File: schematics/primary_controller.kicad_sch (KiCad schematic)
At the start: 0 parts

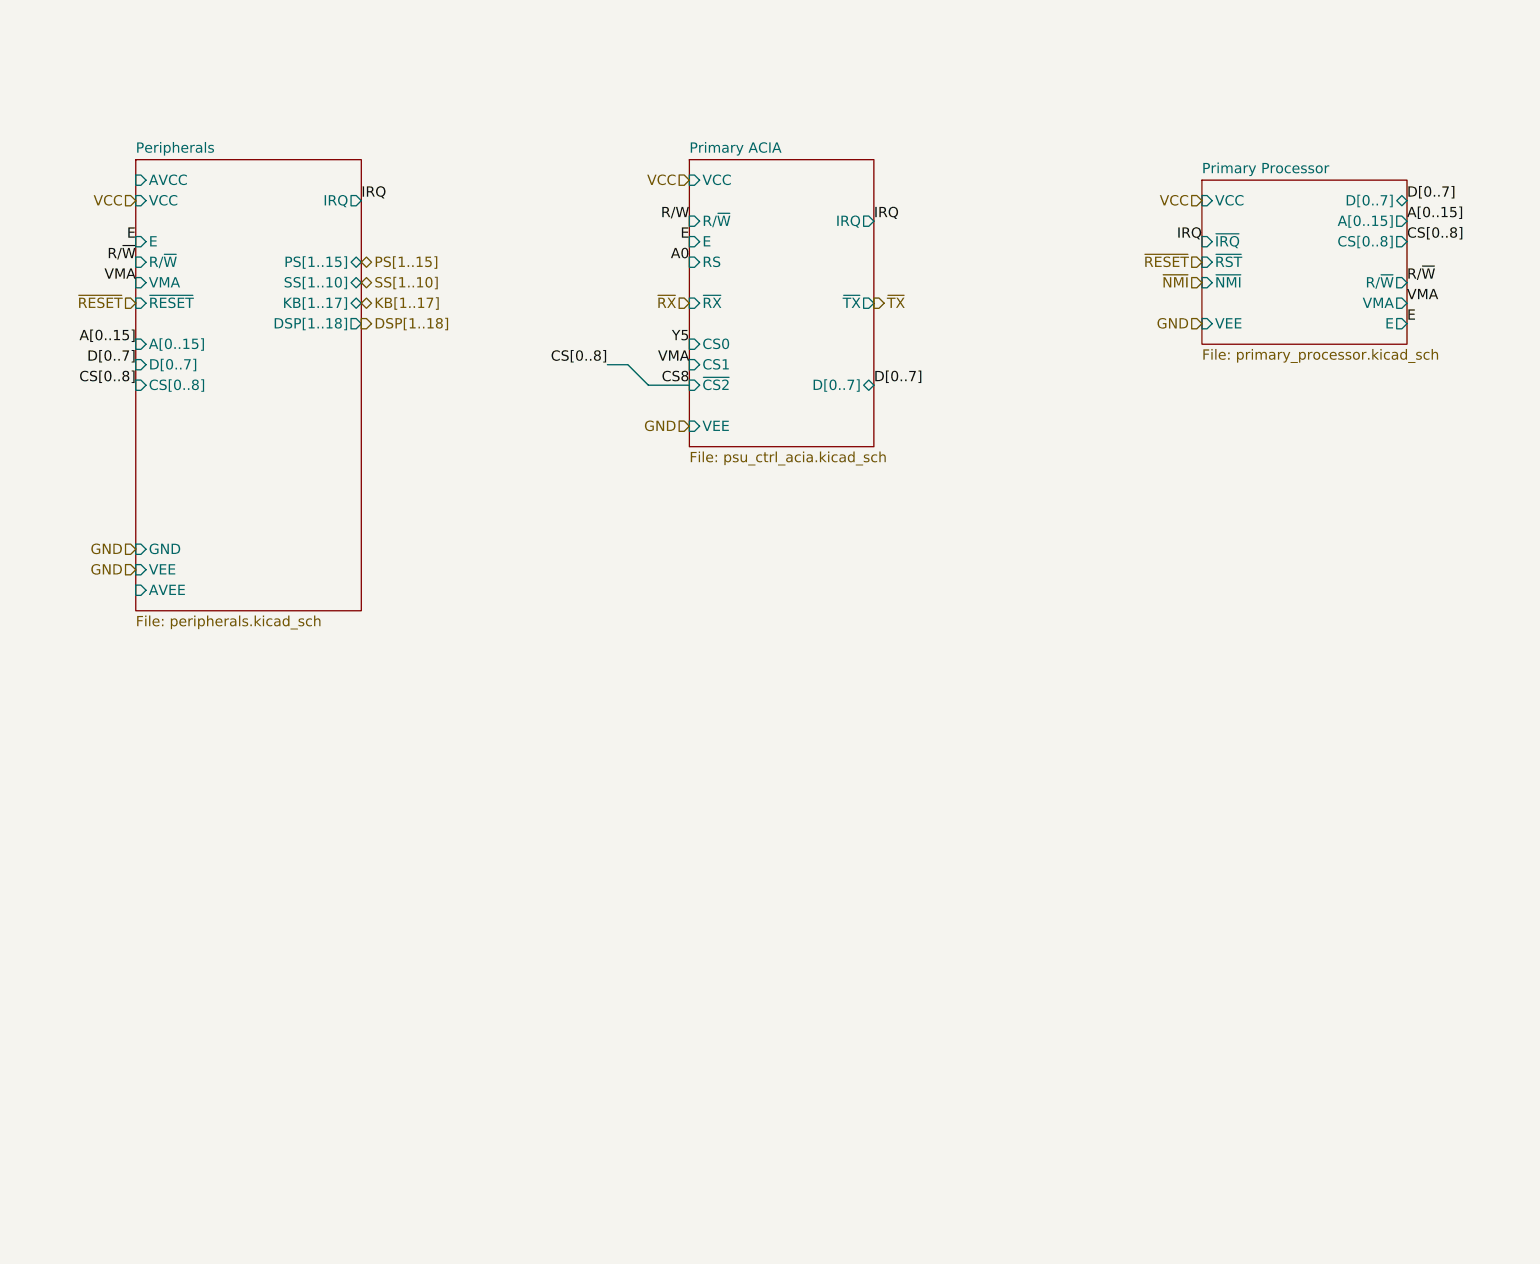
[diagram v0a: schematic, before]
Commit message: Moved more components into hierachical sheets, misc cleanup
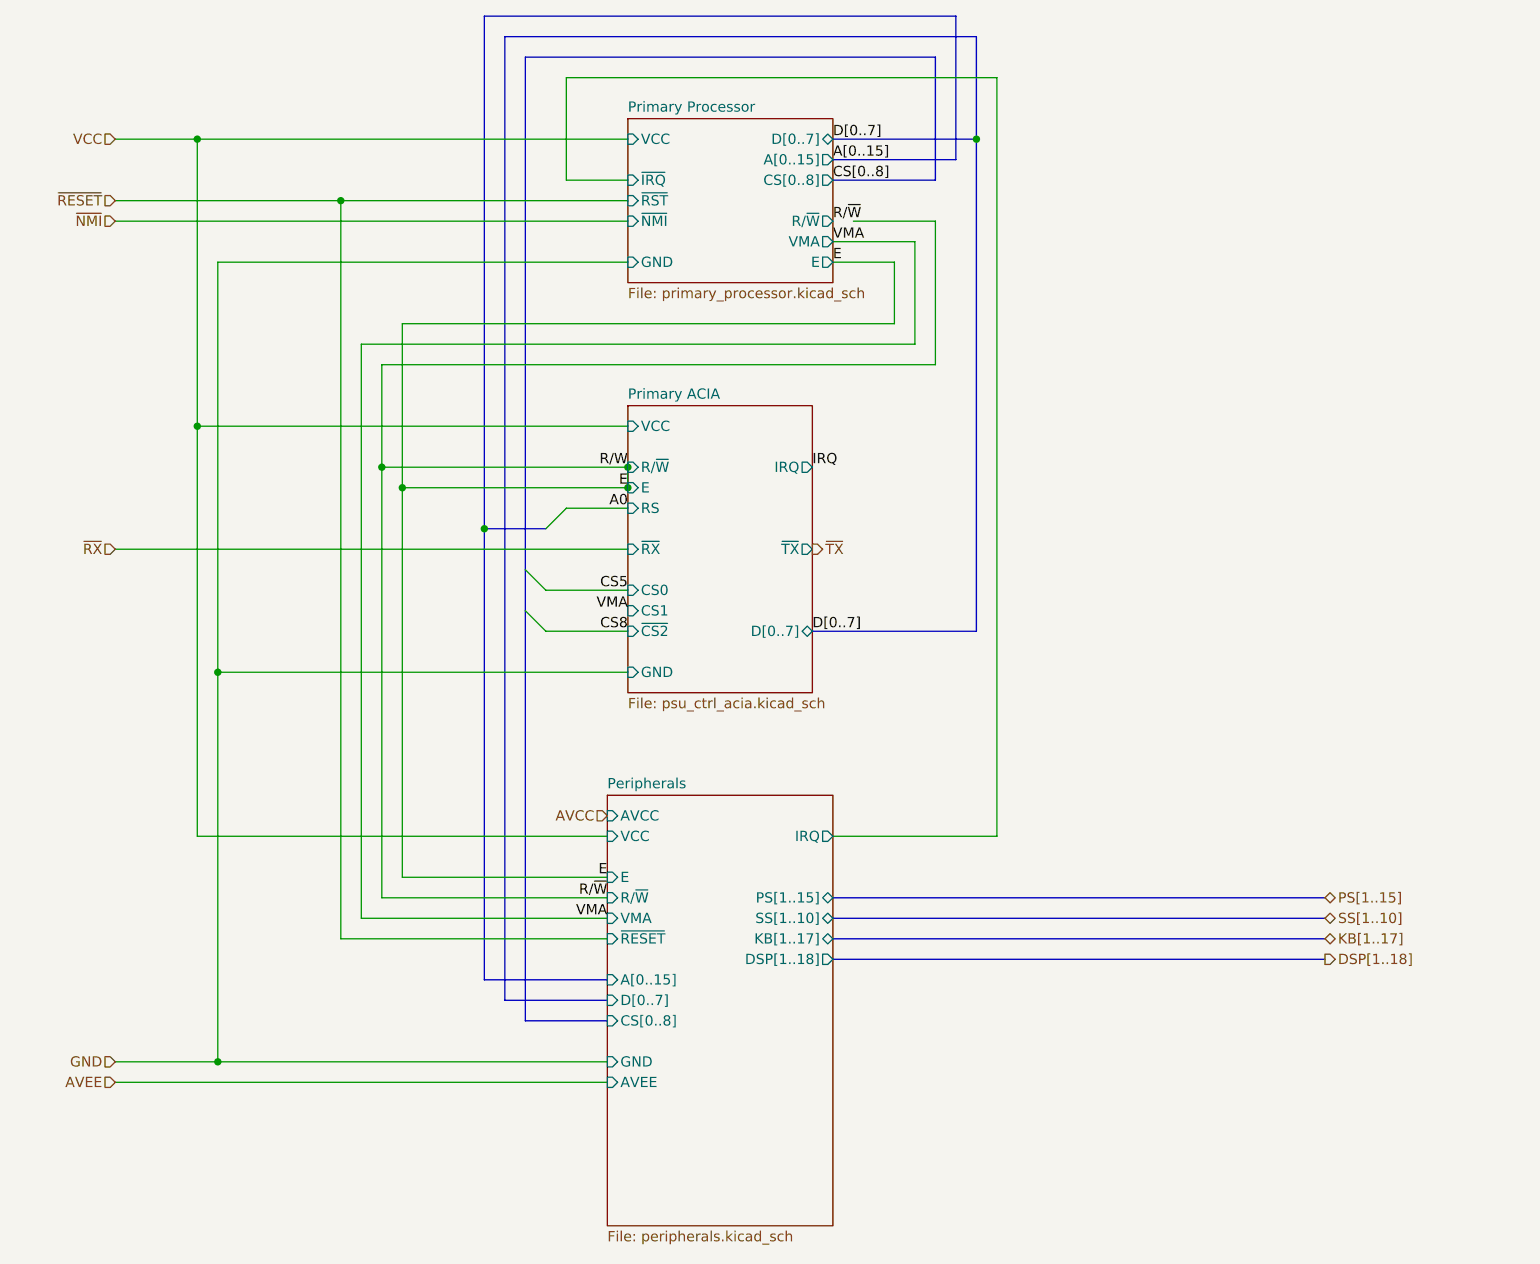
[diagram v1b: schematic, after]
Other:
- sheet Peripherals ports: added none; removed VEE
- sheet Primary ACIA ports: added GND; removed VEE
- sheet Primary Processor ports: added GND; removed VEE

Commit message: cleanup, fixes, started on power supplies
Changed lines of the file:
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@@
 (kicad_sch (version 20211123) (generator eeschema)
   (paper "A4")
-  (junction (at 124.46 76.2) (diameter 0) (color 0 0 0 0)
-  )
   (junction (at 73.66 99.06) (diameter 0) (color 0 0 0 0)
   )
@@
   (junction (at 93.98 73.66) (diameter 0) (color 0 0 0 0)
   )
-  (junction (at 124.46 73.66) (diameter 0) (color 0 0 0 0)
-  )
   (junction (at 106.68 81.28) (diameter 0) (color 0 0 0 0)
   )
@@
   )
   (bus (pts (xy 149.86 132.08) (xy 210.82 132.08))
-    (stroke (width 0) (type default) (color 0 0 0 0))
-  )
-  (wire (pts (xy 124.46 76.2) (xy 124.46 73.66))
     (stroke (width 0) (type default) (color 0 0 0 0))
   )
@@
     )
   )
-  (sheet (at 121.92 114.3) (size 27.94 53.34) (fields_autoplaced)
+  (sheet (at 121.92 114.3) (size 27.94 38.1) (fields_autoplaced)
     (stroke (width 0.1524) (type solid) (color 0 0 0 0))
     (fill (color 0 0 0 0.0000))
@@
       (effects (font (size 1.27 1.27)) (justify left bottom))
     )
-    (property "Sheet file" "peripherals.kicad_sch" (id 1) (at 121.92 168.2246 0)
+    (property "Sheet file" "peripherals.kicad_sch" (id 1) (at 121.92 152.9846 0)
       (effects (font (size 1.27 1.27)) (justify left top))
     )

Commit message: More power supply work
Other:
- sheet Peripherals ports: added SW_RST; removed none
